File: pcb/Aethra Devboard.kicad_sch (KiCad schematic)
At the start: 44 parts, among them J1 USB_C_Receptacle_USB2.0_14P, J2 Conn_01x20, J3 Conn_01x20, J4 Conn_01x03, J5 Conn_01x02, Q1 DMG2301L, SW1 SW_Push, U1 RP2040, U2 AP2112K-3.3, U3 W25Q128JVS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

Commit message: Move kicad files to correct location
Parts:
- removed U3: W25Q128JVS, Package_SO:SOIC-8_5.3x5.3mm_P1.27mm, symbol Memory_Flash:W25Q128JVS
- added U3: W25Q32JVZP, Package_SON:WSON-8-1EP_6x5mm_P1.27mm_EP3.4x4.3mm, symbol Memory_Flash:W25Q32JVZP
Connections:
- net +3V3: now also U3.8 (VCC)
- net GND: now also U3.4 (GND), U3.9 (EP)
- net QSPI_SCLK: now also U3.6 (CLK)
- net QSPI_SD0: now also U3.5 (DI/IO_{0})
- net QSPI_SD1: now also U3.2 (DO/IO_{1})
- net QSPI_SD2: now also U3.3 (~{WP}/IO_{2})
- net QSPI_SD3: now also U3.7 (~{HOLD}/~{RESET}/IO_{3})
- net QSPI_SS: now also U3.1 (~{CS})
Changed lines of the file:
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@@
 	)
 	(junction
+		(at 63.5 182.88)
+		(diameter 0)
+		(color 0 0 0 0)
+	)
+	(junction
 		(at 41.91 110.49)
 		(diameter 0)
@@
 	(wire
 		(pts
+			(xy 63.5 182.88) (xy 66.04 182.88)
+		)
+		(stroke
+			(width 0)
+			(type default)
+		)
+	)
+	(wire
+		(pts
 			(xy 26.67 110.49) (xy 27.94 110.49)
 		)
@@
 	)
 	(symbol
+		(lib_id "Memory_Flash:W25Q32JVZP")
+		(at 63.5 170.18 0)
+		(unit 1)
+		(exclude_from_sim no)
+		(in_bom yes)
+		(on_board yes)
+		(dnp no)
+		(fields_autoplaced yes)
+		(property "Reference" "U3"
+			(at 74.93 168.9099 0)
+			(effects
+				(font
+					(size 1.27 1.27)
+				)
+				(justify left)
+			)
+		)
+		(property "Value" "W25Q32JVZP"
+			(at 74.93 171.4499 0)
+			(effects
+				(font
+					(size 1.27 1.27)
+				)
+				(justify left)
+			)
+		)
+		(property "Footprint" "Package_SON:WSON-8-1EP_6x5mm_P1.27mm_EP3.4x4.3mm"
+			(at 63.5 170.18 0)
+			(effects
+				(font
+					(size 1.27 1.27)
+				)
+				(hide yes)
+			)
+		)
+		(property "Datasheet" "http://www.winbond.com/resource-files/w25q32jv%20revg%2003272018%20plus.pdf"
+			(at 63.5 172.72 0)
+			(effects
+				(font
+					(size 1.27 1.27)
+				)
+				(hide yes)
+			)
+		)
+		(property "Description" "32Mbit / 4MiB Serial Flash Memory, Standard/Dual/Quad SPI, 2.7-3.6V, WSON-8"
+			(at 63.5 170.18 0)
+			(effects
+				(font
+					(size 1.27 1.27)
+				)
+				(hide yes)
+			)
+		)
+		(pin "7"
+		)
+		(pin "2"
+		)
+		(pin "8"
+		)
+		(pin "4"
+		)
+		(pin "6"
+		)
+		(pin "3"
+		)
+		(pin "1"
+		)
+		(pin "5"
+		)
+		(pin "9"
+		)
+		(instances
+			(project ""
+				(path "/096052f6-535c-47de-956e-f78421eba4d9"
+					(reference "U3")
+					(unit 1)
+				)
+			)
+		)
+	)
+	(symbol
 		(lib_id "power:GND")
 		(at 128.27 170.18 0)
@@
 					(unit 1)
 				)
-			)
-		)
-	)
-	(symbol
-		(lib_id "Memory_Flash:W25Q128JVS")
-		(at 63.5 170.18 0)
-		(unit 1)
-		(exclude_from_sim no)
-		(in_bom yes)
-		(on_board yes)
-		(dnp no)
-		(fields_autoplaced yes)
-		(property "Reference" "U3"
-			(at 74.93 168.9099 0)
-			(effects
-				(font
-					(size 1.27 1.27)
-				)
-				(justify left)
-			)
-		)
-		(property "Value" "W25Q128JVS"
-			(at 74.93 171.4499 0)
-			(effects
-				(font
-					(size 1.27 1.27)
-				)
-				(justify left)
-			)
-		)
-		(property "Footprint" "Package_SO:SOIC-8_5.3x5.3mm_P1.27mm"
-			(at 63.5 147.32 0)
-			(effects
-				(font
-					(size 1.27 1.27)
-				)
-				(hide yes)
-			)
-		)
-		(property "Datasheet" "https://www.winbond.com/resource-files/w25q128jv_dtr%20revc%2003272018%20plus.pdf"
-			(at 63.5 144.78 0)
-			(effects
-				(font
-					(size 1.27 1.27)
-				)
-				(hide yes)
-			)
-		)
-		(property "Description" "128Mbit / 16MiB Serial Flash Memory, Standard/Dual/Quad SPI, 2.7-3.6V, SOIC-8"
-			(at 63.5 142.24 0)
-			(effects
-				(font
-					(size 1.27 1.27)
-				)
-				(hide yes)
-			)
-		)
-		(pin "2"
-		)
-		(pin "6"
-		)
-		(pin "1"
-		)
-		(pin "5"
-		)
-		(pin "3"
-		)
-		(pin "7"
-		)
-		(pin "4"
-		)
-		(pin "8"
-		)
-		(instances
-			(project ""
-				(path "/096052f6-535c-47de-956e-f78421eba4d9"
-					(reference "U3")
-					(unit 1)
-				)

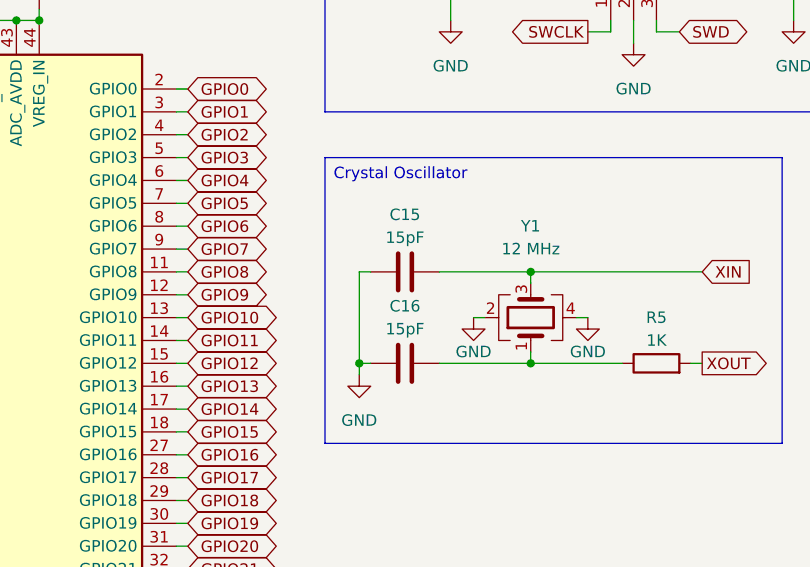
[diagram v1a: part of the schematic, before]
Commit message: Add footprints to components
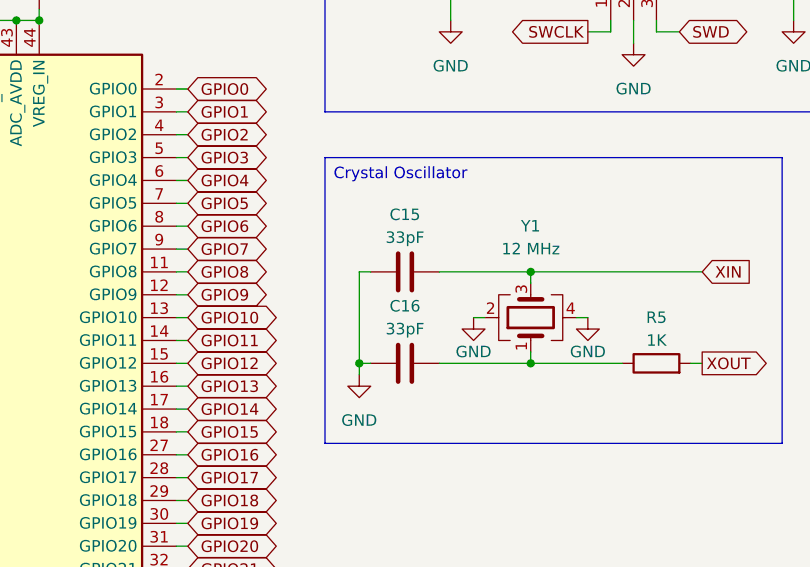
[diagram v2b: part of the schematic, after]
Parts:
- C1, C10, C11, C12, C13, C14, C17, C18, C2, C3, C4, C5, C6, C7, C8, C9: footprint (none) -> Capacitor_SMD:C_0402_1005Metric
- C15, C16: value 15pF -> 33pF; footprint (none) -> Capacitor_SMD:C_0402_1005Metric
- D2: footprint (none) -> LED_SMD:LED_0402_1005Metric
- J1: footprint (none) -> Connector_USB:USB_C_Receptacle_HRO_TYPE-C-31-M-12
- J2, J3: footprint (none) -> Connector_PinHeader_2.54mm:PinHeader_1x20_P2.54mm_Vertical
- J4: footprint (none) -> Connector_JST:JST_SH_BM03B-SRSS-TB_1x03-1MP_P1.00mm_Vertical
- J5: footprint (none) -> Connector_JST:JST_PH_S3B-PH-SM4-TB_1x03-1MP_P2.00mm_Horizontal
- R1, R10, R11, R2, R3, R4, R5, R6, R7, R8, R9: footprint (none) -> Resistor_SMD:R_0402_1005Metric
- SW1: footprint (none) -> Button_Switch_SMD:SW_Push_SPST_NO_Alps_SKRK
- Y1: footprint (none) -> Crystal:Crystal_SMD_3225-4Pin_3.2x2.5mm
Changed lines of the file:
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@@
 			)
 		)
-		(property "Footprint" ""
+		(property "Footprint" "Capacitor_SMD:C_0402_1005Metric"
 			(at 32.7152 119.38 0)
 			(effects
@@
 			)
 		)
-		(property "Footprint" ""
+		(property "Footprint" "Resistor_SMD:R_0402_1005Metric"
 			(at 16.002 116.84 90)
 			(effects
@@
 			)
 		)
-		(property "Footprint" ""
+		(property "Footprint" "Capacitor_SMD:C_0402_1005Metric"
 			(at 82.2452 63.5 0)
 			(effects
@@
 			)
 		)
-		(property "Footprint" ""
+		(property "Footprint" "Capacitor_SMD:C_0402_1005Metric"
 			(at 89.8652 63.5 0)
 			(effects
@@
 			)
 		)
-		(property "Footprint" ""
+		(property "Footprint" "Crystal:Crystal_SMD_3225-4Pin_3.2x2.5mm"
 			(at 193.04 110.49 0)
 			(effects
@@
 			)
 		)
-		(property "Footprint" ""
+		(property "Footprint" "Resistor_SMD:R_0402_1005Metric"
 			(at 90.17 38.862 90)
 			(effects
@@
 			)
 		)
-		(property "Value" "15pF"
+		(property "Value" "33pF"
 			(at 179.07 101.6 90)
 			(effects
@@
 			)
 		)
-		(property "Footprint" ""
+		(property "Footprint" "Capacitor_SMD:C_0402_1005Metric"
 			(at 182.88 104.4448 0)
 			(effects
@@
 			)
 		)
-		(property "Footprint" ""
+		(property "Footprint" "Capacitor_SMD:C_0402_1005Metric"
 			(at 70.8152 119.38 0)
 			(effects
@@
 			)
 		)
-		(property "Footprint" ""
+		(property "Footprint" "Capacitor_SMD:C_0402_1005Metric"
 			(at 106.3752 63.5 0)
 			(effects
@@
 			)
 		)
-		(property "Footprint" ""
+		(property "Footprint" "LED_SMD:LED_0402_1005Metric"
 			(at 101.6 25.4 0)
 			(effects
@@
 			)
 		)
-		(property "Footprint" ""
+		(property "Footprint" "Connector_JST:JST_PH_S3B-PH-SM4-TB_1x03-1MP_P2.00mm_Horizontal"
 			(at 146.05 30.48 0)
 			(effects
@@
 			)
 		)
-		(property "Footprint" ""
+		(property "Footprint" "Capacitor_SMD:C_0402_1005Metric"
 			(at 98.7552 63.5 0)
 			(effects
@@
 			)
 		)
-		(property "Footprint" ""
+		(property "Footprint" "Capacitor_SMD:C_0402_1005Metric"
 			(at 159.7152 63.5 0)
 			(effects
@@
 			)
 		)
-		(property "Footprint" ""
+		(property "Footprint" "Capacitor_SMD:C_0402_1005Metric"
 			(at 121.6152 63.5 0)
 			(effects
@@
 			)
 		)
-		(property "Footprint" ""
+		(property "Footprint" "Capacitor_SMD:C_0402_1005Metric"
 			(at 144.4752 63.5 0)
 			(effects
@@
 			)
 		)
-		(property "Footprint" ""
+		(property "Footprint" "Capacitor_SMD:C_0402_1005Metric"
 			(at 152.0952 63.5 0)
 			(effects
@@
 			)
 		)
-		(property "Footprint" ""
+		(property "Footprint" "Button_Switch_SMD:SW_Push_SPST_NO_Alps_SKRK"
 			(at 24.13 157.48 0)
 			(effects
@@
 			)
 		)
-		(property "Footprint" ""
+		(property "Footprint" "Resistor_SMD:R_0402_1005Metric"
 			(at 34.29 164.338 90)
 			(effects
@@
 			)
 		)
-		(property "Footprint" ""
+		(property "Footprint" "Resistor_SMD:R_0402_1005Metric"
 			(at 43.688 114.3 90)
 			(effects
@@
 			)
 		)
-		(property "Footprint" ""
+		(property "Footprint" "Resistor_SMD:R_0402_1005Metric"
 			(at 97.79 97.028 90)
 			(effects
@@
 			)
 		)
-		(property "Value" "15pF"
+		(property "Value" "33pF"
 			(at 179.07 111.76 90)
 			(effects
@@
 			)
 		)
-		(property "Footprint" ""
+		(property "Footprint" "Capacitor_SMD:C_0402_1005Metric"
 			(at 182.88 114.6048 0)
 			(effects
@@
 			)
 		)
-		(property "Footprint" ""
+		(property "Footprint" "Resistor_SMD:R_0402_1005Metric"
 			(at 97.79 94.488 90)
 			(effects
@@
 			)
 		)
-		(property "Footprint" ""
+		(property "Footprint" "Capacitor_SMD:C_0402_1005Metric"
 			(at 129.2352 63.5 0)
 			(effects
@@
 			)
 		)
-		(property "Footprint" ""
+		(property "Footprint" "Connector_JST:JST_SH_BM03B-SRSS-TB_1x03-1MP_P1.00mm_Vertical"
 			(at 204.47 72.39 0)
 			(effects
@@
 			)
 		)
-		(property "Footprint" ""
+		(property "Footprint" "Capacitor_SMD:C_0402_1005Metric"
 			(at 136.8552 63.5 0)
 			(effects
@@
 			)
 		)
-		(property "Footprint" ""
+		(property "Footprint" "Resistor_SMD:R_0402_1005Metric"
 			(at 52.07 34.798 90)
 			(effects
@@
 			)
 		)
-		(property "Footprint" ""
+		(property "Footprint" "Connector_PinHeader_2.54mm:PinHeader_1x20_P2.54mm_Vertical"
 			(at 215.9 48.26 0)
 			(effects
@@
 			)
 		)
-		(property "Footprint" ""
+		(property "Footprint" "Resistor_SMD:R_0402_1005Metric"
 			(at 110.49 23.622 90)
 			(effects
@@
 			)
 		)
-		(property "Footprint" ""
+		(property "Footprint" "Connector_PinHeader_2.54mm:PinHeader_1x20_P2.54mm_Vertical"
 			(at 190.5 48.26 0)
 			(effects
@@
 			)
 		)
-		(property "Footprint" ""
+		(property "Footprint" "Resistor_SMD:R_0402_1005Metric"
 			(at 52.07 28.702 90)
 			(effects
@@
 			)
 		)
-		(property "Footprint" ""
+		(property "Footprint" "Capacitor_SMD:C_0402_1005Metric"
 			(at 124.1552 39.37 0)
 			(effects
@@
 			)
 		)
-		(property "Footprint" ""
+		(property "Footprint" "Connector_USB:USB_C_Receptacle_HRO_TYPE-C-31-M-12"
 			(at 34.29 40.64 0)
 			(effects
@@
 			)
 		)
-		(property "Footprint" ""
+		(property "Footprint" "Capacitor_SMD:C_0402_1005Metric"
 			(at 73.66 150.1648 0)
 			(effects
@@
 			)
 		)
-		(property "Footprint" ""
+		(property "Footprint" "Capacitor_SMD:C_0402_1005Metric"
 			(at 74.6252 63.5 0)
 			(effects
@@
 			)
 		)
-		(property "Footprint" ""
+		(property "Footprint" "Capacitor_SMD:C_0402_1005Metric"
 			(at 113.9952 63.5 0)
 			(effects
@@
 			)
 		)
-		(property "Footprint" ""
+		(property "Footprint" "Resistor_SMD:R_0402_1005Metric"
 			(at 42.672 157.48 90)
 			(effects
@@
 			)
 		)
-		(property "Footprint" ""
+		(property "Footprint" "Resistor_SMD:R_0402_1005Metric"
 			(at 207.01 117.348 90)
 			(effects

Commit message: Finish routing PCB
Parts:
- J5: footprint Connector_JST:JST_PH_S3B-PH-SM4-TB_1x03-1MP_P2.00mm_Horizontal -> Connector_JST:JST_PH_S2B-PH-SM4-TB_1x02-1MP_P2.00mm_Horizontal
- U3: value W25Q32JVZP -> W25Q16JVZPIQ; footprint Package_SON:WSON-8-1EP_6x5mm_P1.27mm_EP3.4x4.3mm -> Package_SON:Winbond_USON-8-1EP_3x2mm_P0.5mm_EP0.2x1.6mm
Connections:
- no-connect marks 0 -> 1
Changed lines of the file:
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@@
 		(color 0 0 0 0)
 	)
+	(no_connect
+		(at 255.27 111.76)
+	)
 	(wire
 		(pts
@@
 			)
 		)
-		(property "Value" "W25Q32JVZP"
+		(property "Value" "W25Q16JVZPIQ"
 			(at 74.93 171.4499 0)
 			(effects
@@
 			)
 		)
-		(property "Footprint" "Package_SON:WSON-8-1EP_6x5mm_P1.27mm_EP3.4x4.3mm"
+		(property "Footprint" "Package_SON:Winbond_USON-8-1EP_3x2mm_P0.5mm_EP0.2x1.6mm"
 			(at 63.5 170.18 0)
 			(effects
@@
 			)
 		)
-		(property "Footprint" "Connector_JST:JST_PH_S3B-PH-SM4-TB_1x03-1MP_P2.00mm_Horizontal"
+		(property "Footprint" "Connector_JST:JST_PH_S2B-PH-SM4-TB_1x02-1MP_P2.00mm_Horizontal"
 			(at 146.05 30.48 0)
 			(effects
